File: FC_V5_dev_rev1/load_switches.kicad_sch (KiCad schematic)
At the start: 20 parts, among them U19 AP22652, U21 AP22652, U22 AP22652, U23 AP22652, U24 AP22652

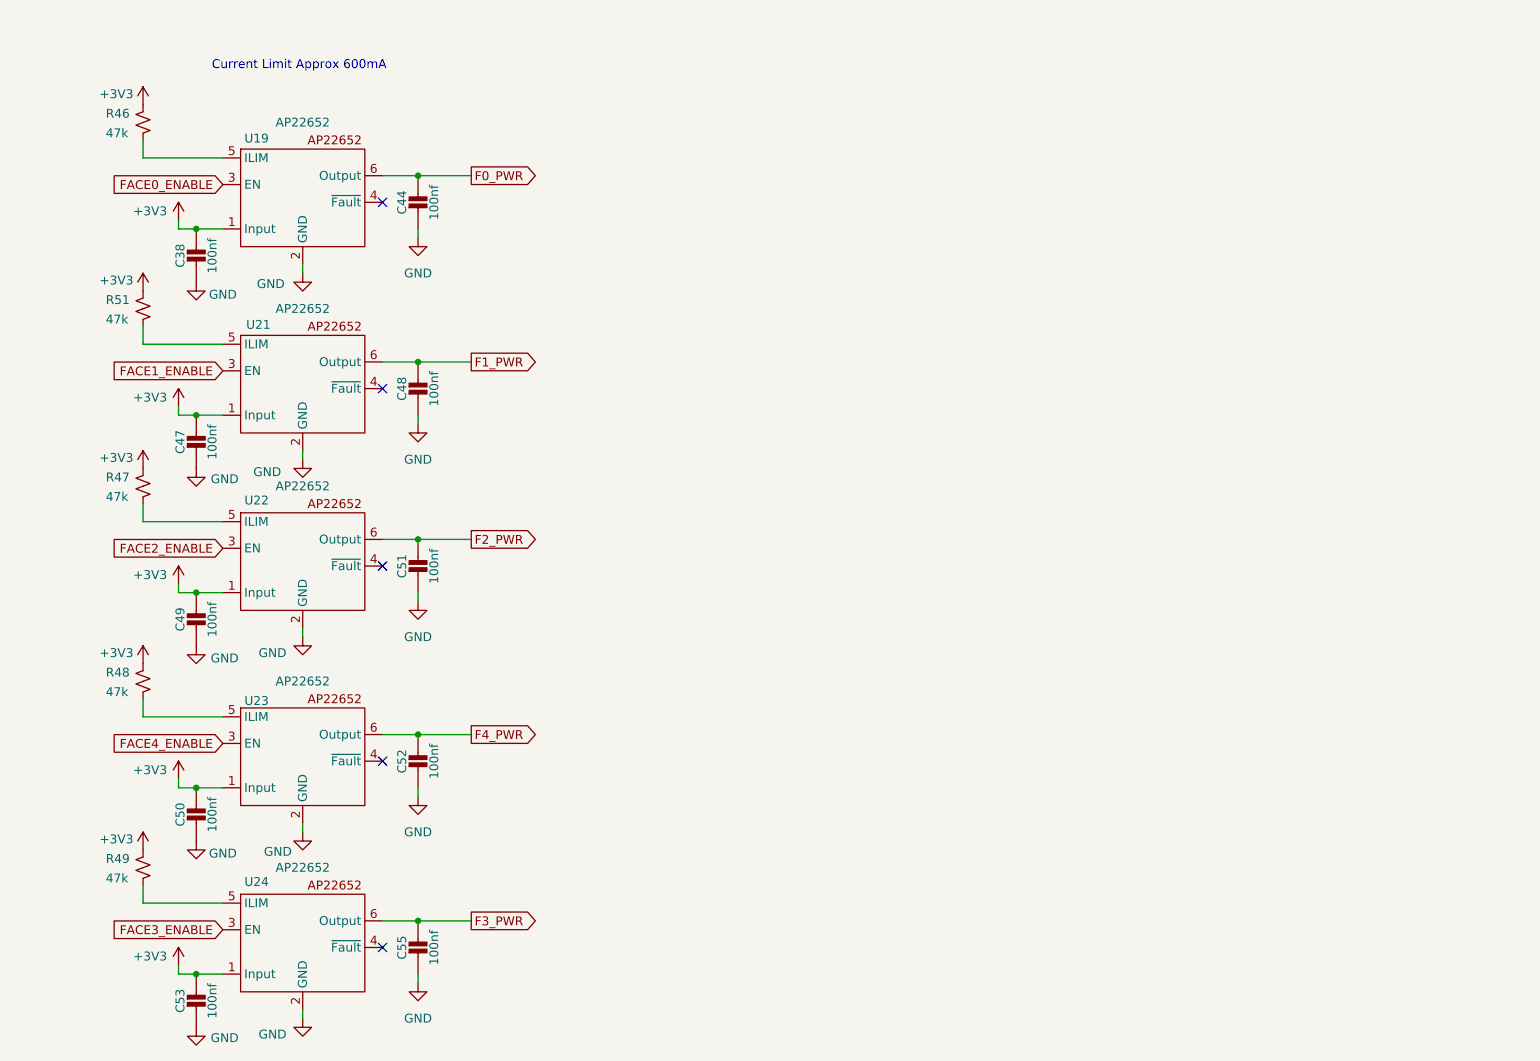
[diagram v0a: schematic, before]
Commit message: Created New AP22652W6-7 Symbol
Also corrected the incorrectly pulled ILIM resistor
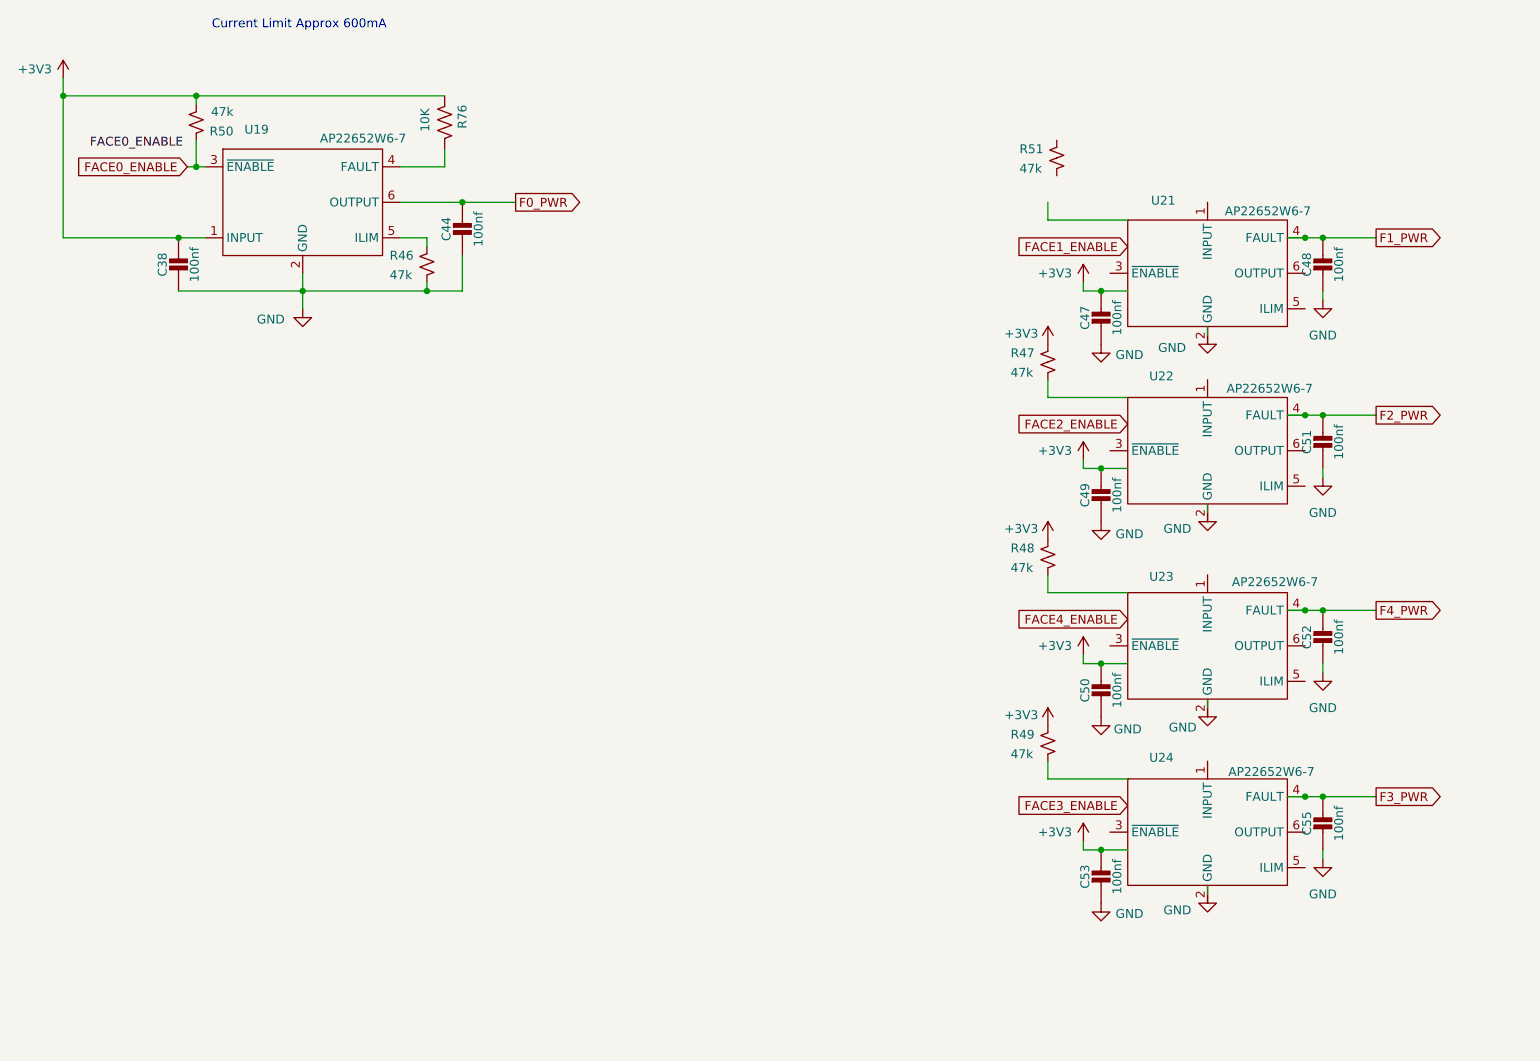
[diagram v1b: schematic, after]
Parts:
- added R50: 47k, Resistor_SMD:R_0603_1608Metric, symbol Device:R_Small_US
- added R76: 10K, Resistor_SMD:R_0603_1608Metric, symbol Device:R_US
- U19, U21, U22, U23, U24: value AP22652 -> AP22652W6-7; footprint SOT26:SOT26 -> AP22652W6-7:SOT-23-6_L2.9-W1.6-P0.95-LS2.8-BL; symbol Power_Management:AP22652 -> PROVES:AP22652W6-7
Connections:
- net +3V3: now also R50.2, R76.1; no longer R46.1, R51.1, U21.1 (Input), U22.1 (Input), U23.1 (Input), U24.1 (Input)
- net F1_PWR: now also U21.4 (FAULT); no longer U21.6 (Output)
- net F2_PWR: now also U22.4 (FAULT); no longer U22.6 (Output)
- net F3_PWR: now also U24.4 (FAULT); no longer U24.6 (Output)
- net F4_PWR: now also U23.4 (FAULT); no longer U23.6 (Output)
- net FACE0_ENABLE: now also R50.1
- net FACE1_ENABLE: no longer U21.3 (EN)
- net FACE2_ENABLE: no longer U22.3 (EN)
- net FACE3_ENABLE: no longer U24.3 (EN)
- net FACE4_ENABLE: no longer U23.3 (EN)
- net GND: now also R46.2; no longer U21.2 (GND), U22.2 (GND), U23.2 (GND), U24.2 (GND)
- net at R47.2: no longer U22.5 (ILIM)
- net at U23.5 (ILIM): no longer R48.2
- net at R49.2: no longer U24.5 (ILIM)
- net at U21.5 (ILIM): no longer R51.2
- net at U19.4 (FAULT): now also R76.2
- net at U19.5 (ILIM): now also R46.1; no longer R46.2
- no-connect marks 5 -> 0
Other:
- moved on the sheet: C38, C44, C47, C48, C49, C50, C51, C52, C53, C55, R46, R47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

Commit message: Updated Loadswitch Schematics
Much cleaner looking now!
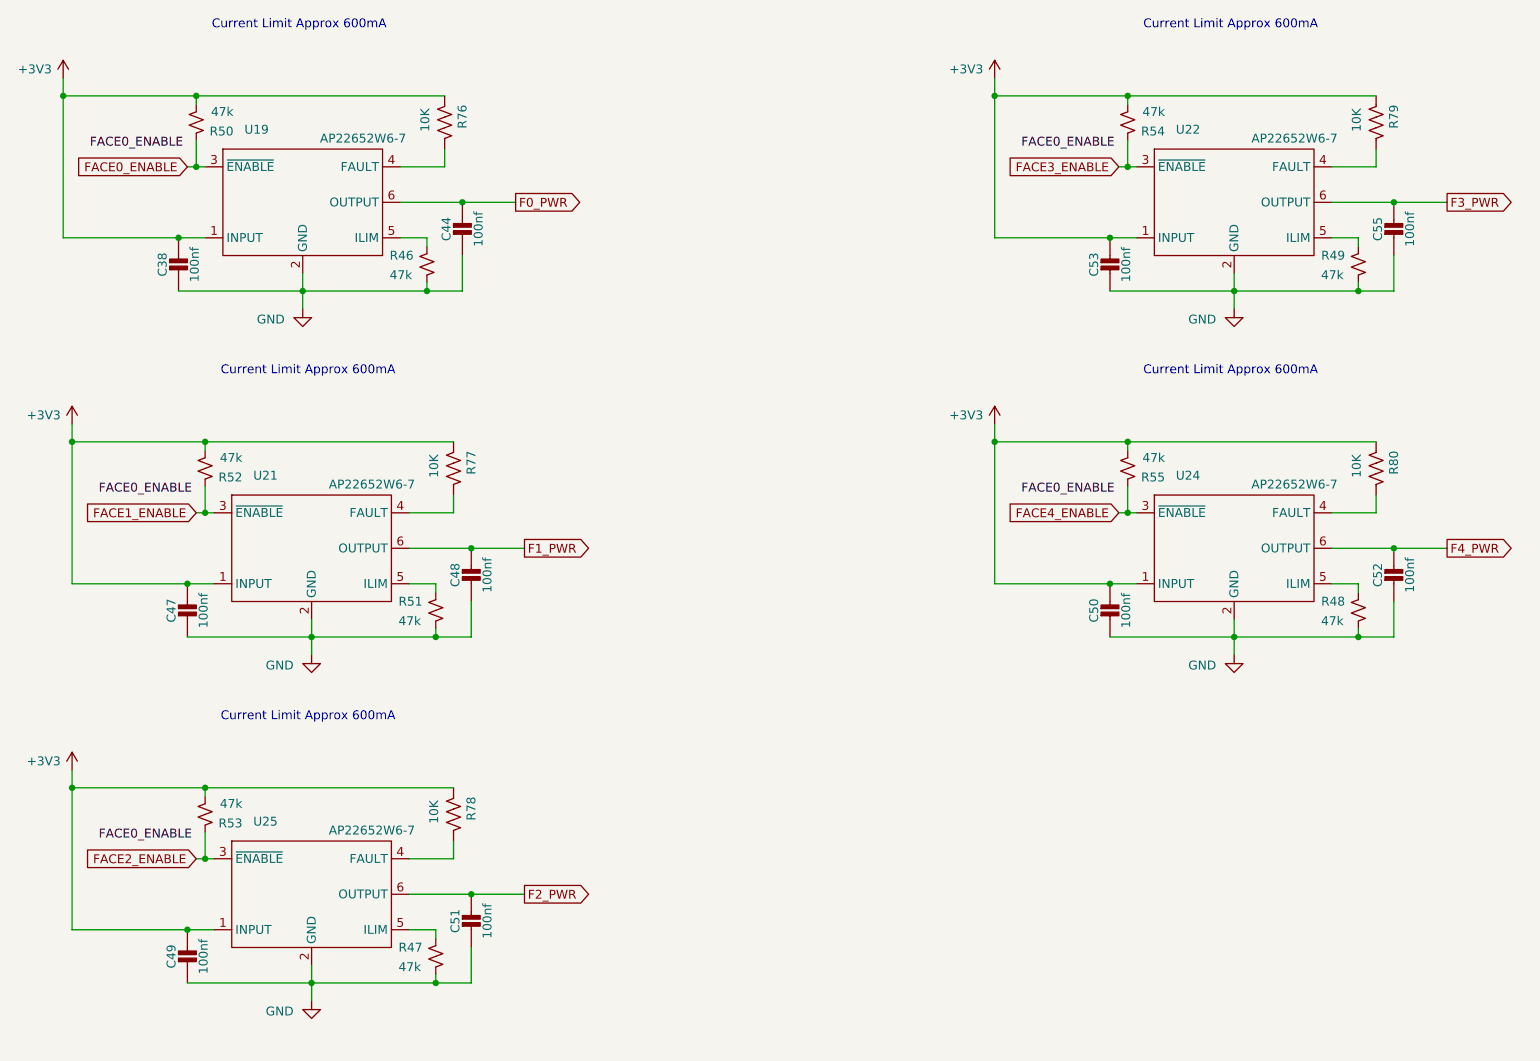
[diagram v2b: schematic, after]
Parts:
- removed U23: AP22652W6-7, AP22652W6-7:SOT-23-6_L2.9-W1.6-P0.95-LS2.8-BL, symbol PROVES:AP22652W6-7
- added R52, R53, R54, R55: 47k, Resistor_SMD:R_0603_1608Metric, symbol Device:R_Small_US
- added R77, R78, R79, R80: 10K, Resistor_SMD:R_0603_1608Metric, symbol Device:R_US
- added U25: AP22652W6-7, AP22652W6-7:SOT-23-6_L2.9-W1.6-P0.95-LS2.8-BL, symbol PROVES:AP22652W6-7
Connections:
- net +3V3: now also U21.1 (INPUT), U22.1 (INPUT), U24.1 (INPUT), R52.2, R53.2, R54.2, R55.2, R77.1, R78.1, R79.1, R80.1, U25.1 (INPUT); no longer R47.1, R48.1, R49.1
- net F1_PWR: now also U21.6 (OUTPUT); no longer U21.4 (FAULT)
- net F2_PWR: now also U25.6 (OUTPUT); no longer U22.4 (FAULT)
- net F3_PWR: now also U22.6 (OUTPUT); no longer U24.4 (FAULT)
- net F4_PWR: now also U24.6 (OUTPUT)
- net FACE1_ENABLE: now also U21.3 (~{ENABLE}), R52.1
- net FACE2_ENABLE: now also R53.1, U25.3 (~{ENABLE})
- net FACE3_ENABLE: now also U22.3 (~{ENABLE}), R54.1
- net FACE4_ENABLE: now also U24.3 (~{ENABLE}), R55.1
- net GND: now also R47.2, R48.2, R49.2, R51.2, U21.2 (GND), U22.2 (GND), U24.2 (GND), U25.2 (GND)
- net at U22.5 (ILIM): now also R49.1
- net at U24.5 (ILIM): now also R48.1
- net at U21.5 (ILIM): now also R51.1
- new net: R80.2, U24.4 (FAULT)
- new net: R77.2, U21.4 (FAULT)
- new net: R79.2, U22.4 (FAULT)
- new net: R78.2, U25.4 (FAULT)
- new net: R47.1, U25.5 (ILIM)
